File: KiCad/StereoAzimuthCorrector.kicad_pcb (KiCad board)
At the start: 2 copper layers, 71.1 x 71.1 mm, 54 parts, among them P1 12VDC_IN, P4 MONO_OUT, P5 HOLE, P6 HOLE, P7 HOLE, P8 HOLE, U1 TL064, U2 L78L09ACZ, U3 TL062

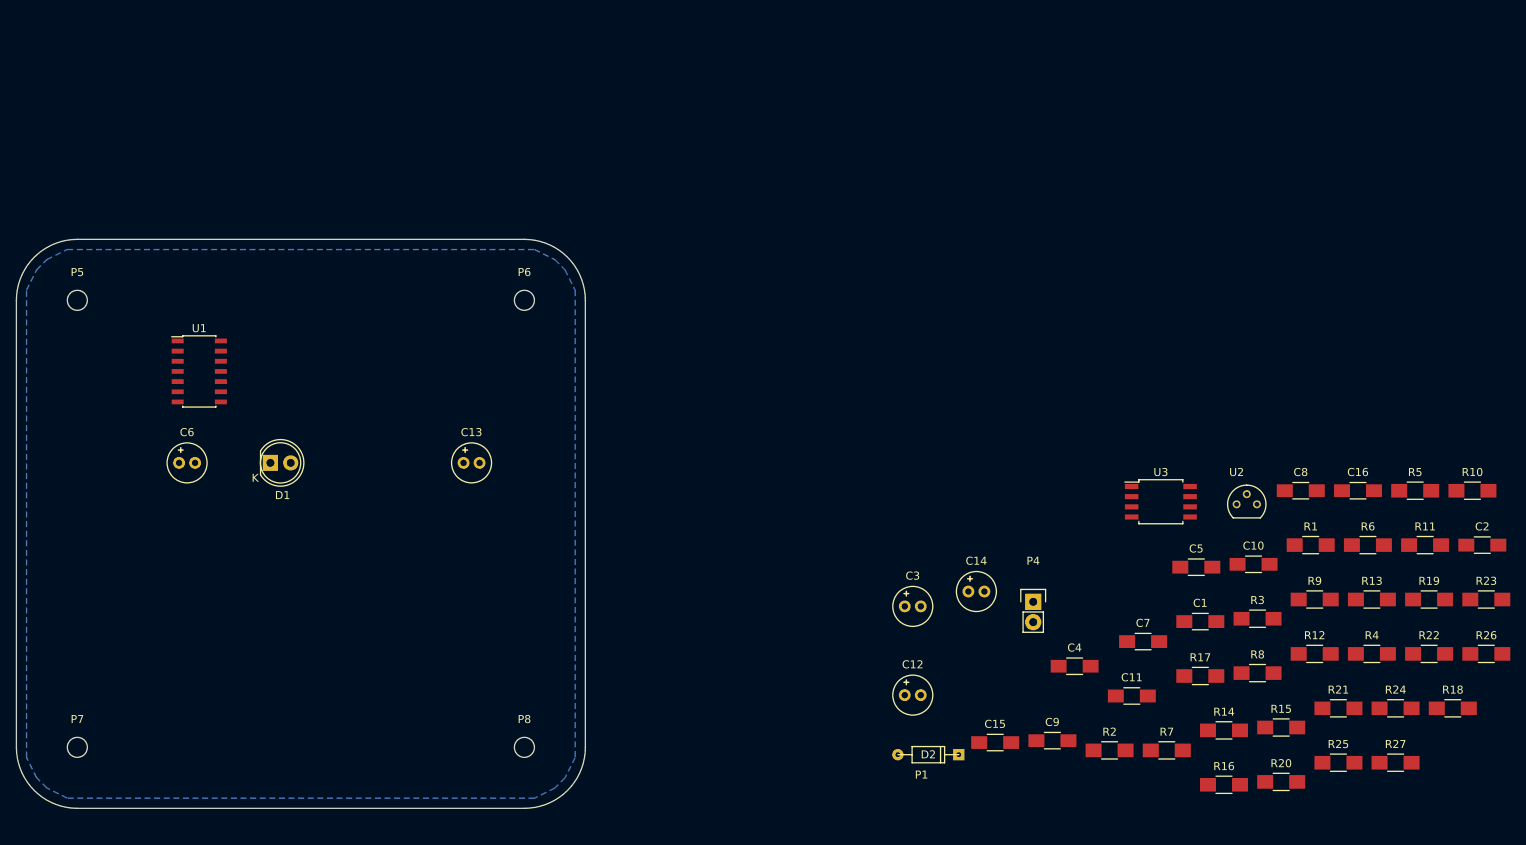
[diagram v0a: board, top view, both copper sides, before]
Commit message: Rough in component placement
Power jack footprint is still TODO
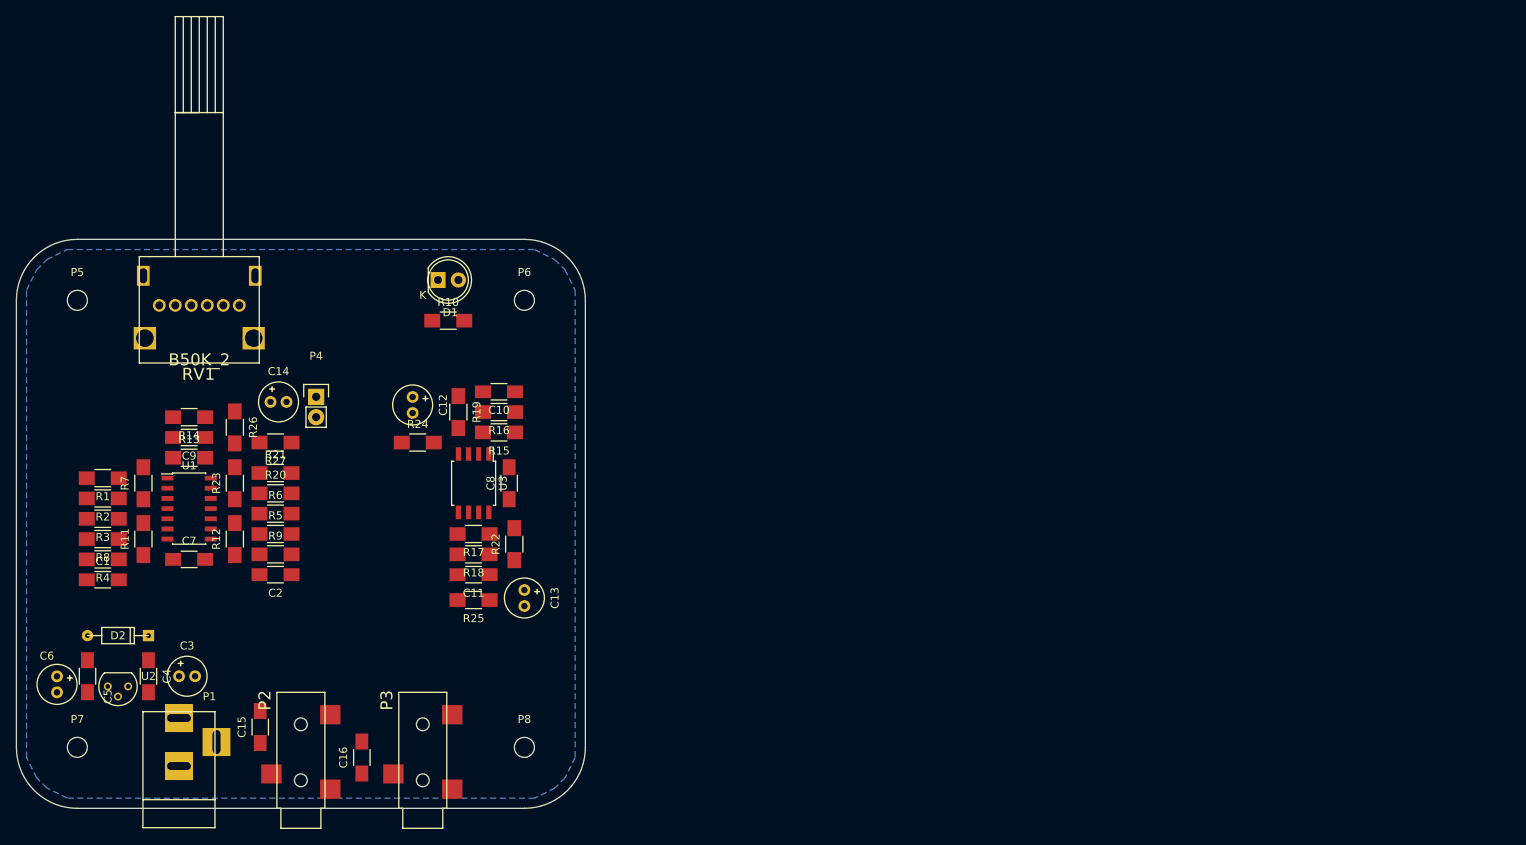
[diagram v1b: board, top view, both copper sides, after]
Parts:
- added P2: SAC_P_3.5MM, SAC_footprints:SAC_P_3.5MM, F.Cu at (52.1, 90.2)
- added P3: SAC_P_3.5MM, SAC_footprints:SAC_P_3.5MM, F.Cu at (67.3, 90.2)
- added RV1: B50K_2, SAC_footprints:SAC_RV1, F.Cu at (39.4, 27.3)
- D1: footprint LEDs:LED-5MM -> SAC_footprints:SAC_LED-5MM
- D2: footprint Discret:DO-35 -> SAC_footprints:SAC_DO-35
- P1: footprint Oddities:Dummy_Empty -> Connect:BARREL_JACK
- moved R11 160.2 mm to (32.4, 56.5), turned to 90 degrees
- moved R4 159.1 mm to (27.3, 59.1), turned to 180 degrees
- moved R26 159.0 mm to (43.8, 42.5), turned to 270 degrees
- moved R23 157.1 mm to (43.8, 49.5), turned to 90 degrees
- moved R1 151.2 mm to (27.3, 48.9), turned to 180 degrees
- moved C2 150.9 mm to (48.9, 61.0), turned to 180 degrees
- moved R13 148.9 mm to (38.1, 46.4)
- moved R27 145.6 mm to (48.9, 44.5), turned to 180 degrees
- moved R8 145.3 mm to (27.3, 56.5), turned to 180 degrees
- moved R3 144.9 mm to (27.3, 54.0), turned to 180 degrees
- moved R5 142.6 mm to (48.9, 55.9)
- moved U2 140.4 mm to (30.5, 74.9), turned to 180 degrees
- moved C5 139.3 mm to (25.4, 73.7), turned to 270 degrees
- moved C1 137.3 mm to (27.3, 61.6)
- moved R6 136.6 mm to (48.9, 53.3)
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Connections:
- P5 pad 1: GND -> Net-(P5-Pad1)
- P6 pad 1: GND -> Net-(P6-Pad1)
- P7 pad 1: GND -> Net-(P7-Pad1)
- P8 pad 1: GND -> Net-(P8-Pad1)
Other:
- net class Power added: clearance 0.254, trace_width 0.762, via_dia 0.889, via_drill 0.635
- board text added: "Check that P1 and RV1 will not interfere with angled case wall"
